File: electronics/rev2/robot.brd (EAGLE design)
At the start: 170.3 x 155.9 mm, 93 parts, among them J1 USB-B, J3 B6B-ZR, J4 B6B-ZR, J5 B6B-ZR, J6 KICKER, Q1 IRLMS2002TRPBF, Q2 IRLMS2002TRPBF, Q3 NPN_BC817,215, Q4 SUD50N04-8M8P-4GE3, Q5 NPN_BC817,215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

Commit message: Re-camming, minor renamings
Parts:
- renumbered U$1 to SW1, U$12 to U11, U$13 to U12, U$25 to U8, U$7 to U10
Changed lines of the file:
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@@
 <attribute name="VALUE" value="0.3" x="-10.16" y="-65.5574" size="1.778" layer="27" display="off"/>
 </element>
-<element name="U$25" library="rhoban" package="SOT223" value="TS2940CW-3.3RP" x="7.4676" y="7.7724" rot="R90">
+<element name="U8" library="rhoban" package="SOT223" value="TS2940CW-3.3RP" x="7.4676" y="7.7724" rot="R90">
 <attribute name="FARNELL" value="7261403" x="-3.0734" y="0.5588" size="1.778" layer="27" rot="R90" display="off"/>
 </element>
@@
 <attribute name="VALUE" value="0.33µF" x="26.3144" y="14.7066" size="1.778" layer="27" rot="R180" display="off"/>
 </element>
-<element name="U$1" library="rhoban" package="L102011ML04Q" value="L102011ML04Q" x="39.1409125" y="18.7719375" rot="R210">
+<element name="SW1" library="rhoban" package="L102011ML04Q" value="L102011ML04Q" x="39.1409125" y="18.7719375" rot="R210">
 <attribute name="FARNELL" value="2931770" x="39.1409125" y="18.7719375" size="1.778" layer="27" rot="R210" display="off"/>
 </element>
-<element name="U$7" library="rhoban" package="HSOP8" value="TB67H450FNG" x="4.159615625" y="-10.26823125"/>
+<element name="U10" library="rhoban" package="HSOP8" value="TB67H450FNG" x="4.159615625" y="-10.26823125"/>
 <element name="R19" library="rcl" package="R1206" value="0.33" x="6.593578125" y="-3.92773125"/>
-<element name="U$12" library="rhoban" package="HSOP8" value="TB67H450FNG" x="-7.65661875" y="0.71041875"/>
+<element name="U11" library="rhoban" package="HSOP8" value="TB67H450FNG" x="-7.65661875" y="0.71041875"/>
 <element name="R20" library="rcl" package="R1206" value="0.33" x="-6.08386875" y="7.10789375"/>
-<element name="U$13" library="rhoban" package="HSOP8" value="TB67H450FNG" x="-39.524309375" y="7.266759375" rot="R210"/>
+<element name="U12" library="rhoban" package="HSOP8" value="TB67H450FNG" x="-39.524309375" y="7.266759375" rot="R210"/>
 <element name="R21" library="rcl" package="R1206" value="0.33" x="-37.80135625" y="1.564721875" rot="R210"/>
 <element name="C18" library="SparkFun-Capacitors" package="0805" value="1µF" x="7.802584375" y="-8.766778125" rot="R270">
@@
 <contactref element="C9" pad="2"/>
 <contactref element="C12" pad="2"/>
-<contactref element="U$25" pad="2"/>
-<contactref element="U$25" pad="2"/>
+<contactref element="U8" pad="2"/>
+<contactref element="U8" pad="2"/>
 <contactref element="C13" pad="2"/>
 <contactref element="C14" pad="2"/>
 <contactref element="U1" pad="26"/>
-<contactref element="U$7" pad="1"/>
+<contactref element="U10" pad="1"/>
 <contactref element="R19" pad="2"/>
-<contactref element="U$12" pad="1"/>
+<contactref element="U11" pad="1"/>
 <contactref element="R20" pad="2"/>
-<contactref element="U$13" pad="1"/>
+<contactref element="U12" pad="1"/>
 <contactref element="R21" pad="2"/>
 <contactref element="C18" pad="2"/>
@@
 <contactref element="C3" pad="1"/>
 <contactref element="C17" pad="1"/>
-<contactref element="U$1" pad="P$1"/>
-<contactref element="U$7" pad="5"/>
-<contactref element="U$12" pad="5"/>
-<contactref element="U$13" pad="5"/>
+<contactref element="SW1" pad="P$1"/>
+<contactref element="U10" pad="5"/>
+<contactref element="U11" pad="5"/>
+<contactref element="U12" pad="5"/>
 <contactref element="C18" pad="1"/>
 <contactref element="C21" pad="1"/>
@@
 <signal name="M1A">
 <contactref element="U2" pad="16"/>
-<contactref element="U$7" pad="3"/>
+<contactref element="U10" pad="3"/>
 <wire x1="4.2926" y1="-22.7004" x2="4.2926" y2="-16.93053125" width="0.4064" layer="1"/>
 <wire x1="4.2926" y1="-16.93053125" x2="4.572" y2="-16.256" width="0.4064" layer="1" curve="-45"/>
@@
 <signal name="M1B">
 <contactref element="U2" pad="13"/>
-<contactref element="U$7" pad="2"/>
+<contactref element="U10" pad="2"/>
 <wire x1="3.524615625" y1="-12.86823125" x2="3.556" y2="-12.944" width="0.4064" layer="1" curve="-45"/>
 <wire x1="3.556" y1="-12.944" x2="3.556" y2="-14.986" width="0.4064" layer="1"/>
@@
 <signal name="M2P2" class="1">
 <contactref element="J4" pad="1"/>
-<contactref element="U$12" pad="8"/>
+<contactref element="U11" pad="8"/>
 <wire x1="-9.56161875" y1="3.31041875" x2="-9.525" y2="4.064" width="0.4064" layer="1"/>
 <wire x1="-9.525" y1="4.064" x2="-9.652" y2="6.096" width="0.4064" layer="1" curve="12.716635"/>
@@
 <signal name="M2A">
 <contactref element="U2" pad="28"/>
-<contactref element="U$12" pad="3"/>
+<contactref element="U11" pad="3"/>
 <wire x1="-7.02161875" y1="-1.88958125" x2="-7.02161875" y2="-3.64638125" width="0.4064" layer="1"/>
 <wire x1="-7.02161875" y1="-3.64638125" x2="-6.985" y2="-3.556" width="0.4064" layer="1"/>
@@
 <signal name="M2B">
 <contactref element="U2" pad="30"/>
-<contactref element="U$12" pad="2"/>
+<contactref element="U11" pad="2"/>
 <wire x1="-8.29161875" y1="-1.88958125" x2="-8.29161875" y2="-3.59261875" width="0.4064" layer="1"/>
 <wire x1="-8.29161875" y1="-3.59261875" x2="-8.382" y2="-3.556" width="0.4064" layer="1"/>
@@
 <signal name="M3A">
 <contactref element="U2" pad="36"/>
-<contactref element="U$13" pad="3"/>
+<contactref element="U12" pad="3"/>
 <wire x1="-41.374234375" y1="9.200925" x2="-42.037" y2="10.414" width="0.4064" layer="1"/>
 <via x="-42.037" y="10.414" extent="1-16" drill="0.3" diameter="0.7" shape="octagon"/>
@@
 <signal name="M3B">
 <contactref element="U2" pad="37"/>
-<contactref element="U$13" pad="2"/>
+<contactref element="U12" pad="2"/>
 <via x="-40.894" y="11.049" extent="1-16" drill="0.3" diameter="0.7" shape="octagon"/>
 <wire x1="-40.894" y1="11.176" x2="-40.5351375" y2="10.273815625" width="0.4064" layer="16"/>
@@
 <contactref element="C5" pad="1"/>
 <contactref element="C6" pad="1"/>
-<contactref element="U$25" pad="1"/>
+<contactref element="U8" pad="1"/>
 <contactref element="D3" pad="1"/>
 <wire x1="-1.662" y1="70.993" x2="-5.08" y2="70.993" width="0.4064" layer="1"/>
@@
 <signal name="M1P1" class="1">
 <contactref element="J3" pad="6"/>
-<contactref element="U$7" pad="6"/>
+<contactref element="U10" pad="6"/>
 <wire x1="4.794615625" y1="-7.66823125" x2="4.794615625" y2="-6.762384375" width="0.4064" layer="1"/>
 <wire x1="4.794615625" y1="-6.762384375" x2="5.969" y2="-5.588" width="0.4064" layer="1" curve="-90"/>
@@
 <signal name="M1P2" class="1">
 <contactref element="J3" pad="1"/>
-<contactref element="U$7" pad="8"/>
+<contactref element="U10" pad="8"/>
 <wire x1="2.254615625" y1="-7.66823125" x2="2.254615625" y2="-5.111384375" width="0.4064" layer="1"/>
 <wire x1="2.254615625" y1="-5.111384375" x2="5.969" y2="-1.524" width="0.4064" layer="1" curve="-90"/>
@@
 <signal name="M2P1" class="1">
 <contactref element="J4" pad="6"/>
-<contactref element="U$12" pad="6"/>
+<contactref element="U11" pad="6"/>
 <wire x1="-7.02161875" y1="3.31041875" x2="-6.985" y2="4.445" width="0.4064" layer="1"/>
 <wire x1="-6.985" y1="4.445" x2="-6.223" y2="5.08" width="0.4064" layer="1" curve="-96.691545"/>
@@
 <signal name="M3P2" class="1">
 <contactref element="J5" pad="1"/>
-<contactref element="U$13" pad="8"/>
+<contactref element="U12" pad="8"/>
 <wire x1="-36.574528125" y1="5.967590625" x2="-33.37213125" y2="0.420871875" width="0.4064" layer="1"/>
 <wire x1="-33.37213125" y1="0.420871875" x2="-33.386109375" y2="0.368690625" width="0.4064" layer="1"/>
@@
 <signal name="M3P1" class="1">
 <contactref element="J5" pad="6"/>
-<contactref element="U$13" pad="6"/>
+<contactref element="U12" pad="6"/>
 <wire x1="-38.774234375" y1="4.697590625" x2="-38.227" y2="3.81" width="0.4064" layer="1"/>
 <wire x1="-38.227" y1="3.81" x2="-38.481" y2="3.048" width="0.4064" layer="1" curve="-100.18061"/>
@@
 <contactref element="C14" pad="1"/>
 <contactref element="C13" pad="1"/>
-<contactref element="U$25" pad="3"/>
+<contactref element="U8" pad="3"/>
 <contactref element="B1" pad="P$2"/>
 <contactref element="J3" pad="2"/>
 <contactref element="J4" pad="2"/>
 <contactref element="J5" pad="2"/>
-<contactref element="U$7" pad="4"/>
-<contactref element="U$12" pad="4"/>
-<contactref element="U$13" pad="4"/>
+<contactref element="U10" pad="4"/>
+<contactref element="U11" pad="4"/>
+<contactref element="U12" pad="4"/>
 <wire x1="10.5664" y1="10.0838" x2="12.875346875" y2="10.0838" width="0.6096" layer="1"/>
 <wire x1="12.875346875" y1="10.0838" x2="13.462" y2="9.8408" width="0.6096" layer="1" curve="-45"/>
@@
 <signal name="N$7" class="1">
 <contactref element="J2" pad="2"/>
-<contactref element="U$1" pad="P$2"/>
+<contactref element="SW1" pad="P$2"/>
 <wire x1="17.9947625" y1="18.074834375" x2="19.608809375" y2="16.4607875" width="1.016" layer="16"/>
 <wire x1="19.608809375" y1="16.4607875" x2="21.023025" y2="15.875" width="1.016" layer="16" curve="45.00009"/>
@@
 </signal>
 <signal name="N$18" class="1">
-<contactref element="U$7" pad="7"/>
+<contactref element="U10" pad="7"/>
 <contactref element="R19" pad="1"/>
 <wire x1="3.524615625" y1="-7.66823125" x2="3.524615625" y2="-7.6457625" width="0.4064" layer="1"/>
@@
 </signal>
 <signal name="N$20" class="1">
-<contactref element="U$12" pad="7"/>
+<contactref element="U11" pad="7"/>
 <contactref element="R20" pad="1"/>
 <wire x1="-8.29161875" y1="3.31041875" x2="-8.255" y2="4.318" width="0.4064" layer="1"/>
@@
 </signal>
 <signal name="N$21" class="1">
-<contactref element="U$13" pad="7"/>
+<contactref element="U12" pad="7"/>
 <contactref element="R21" pad="1"/>
 <wire x1="-37.67438125" y1="5.332590625" x2="-36.83" y2="3.81" width="0.4064" layer="1"/>

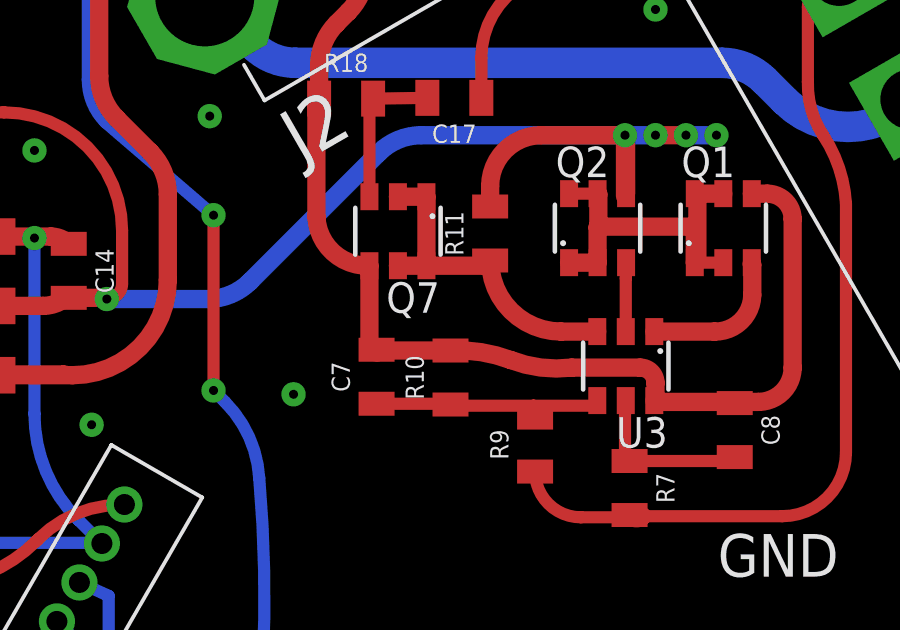
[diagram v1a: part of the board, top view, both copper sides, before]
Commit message: Adding D2 diode
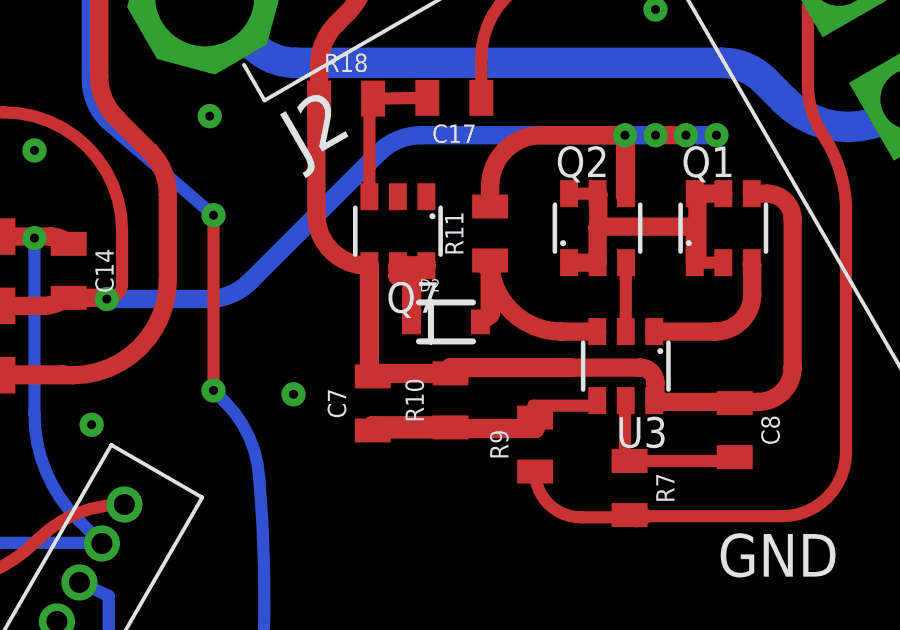
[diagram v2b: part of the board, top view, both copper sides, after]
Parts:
- added D2: (no value), SparkFun-DiscreteSemi:SOD-323
- moved C7 0.90 mm to (23.6, 4.52)
- moved R10 0.76 mm to (26.2, 4.62)
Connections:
- new net N$22: D2.1, Q7.1, Q7.2, Q7.5, Q7.6
- net N$13: now also D2.2; no longer Q7.1, Q7.2, Q7.5, Q7.6
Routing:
- net N$13: track 10.9 -> 7.00 mm
- net N$22: track 0.00 -> 3.28 mm
- net GND_RAW: track 38.8 -> 39.7 mm
- net N$9: track 7.94 -> 8.65 mm
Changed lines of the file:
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@@
 <attribute name="FARNELL" value="2074334RL" x="29.0068" y="3.1496" size="1.778" layer="27" rot="R90" display="off"/>
 </element>
-<element name="R10" library="SparkFun-Resistors" package="0805" value="470" x="26.1874" y="5.3848" rot="R90">
-<attribute name="PROD_ID" value="RES-11622" x="26.1874" y="5.3848" size="1.778" layer="27" rot="R90" display="off"/>
-<attribute name="VALUE" value="0.3" x="26.1874" y="5.3848" size="1.778" layer="27" rot="R90" display="off"/>
-<attribute name="FARNELL" value="2074334RL" x="26.1874" y="5.3848" size="1.778" layer="27" rot="R90" display="off"/>
+<element name="R10" library="SparkFun-Resistors" package="0805" value="470" x="26.1874" y="4.6228" rot="R90">
+<attribute name="PROD_ID" value="RES-11622" x="26.1874" y="4.6228" size="1.778" layer="27" rot="R90" display="off"/>
+<attribute name="VALUE" value="0.3" x="26.1874" y="4.6228" size="1.778" layer="27" rot="R90" display="off"/>
+<attribute name="FARNELL" value="2074334RL" x="26.1874" y="4.6228" size="1.778" layer="27" rot="R90" display="off"/>
 </element>
 <element name="R11" library="SparkFun-Resistors" package="0805" value="2K" x="27.5082" y="10.1854" rot="R90">
@@
 <attribute name="FARNELL" value="2688486RL" x="-0.762" y="70.993" size="1.778" layer="27" display="off"/>
 </element>
-<element name="C7" library="SparkFun-Capacitors" package="0805" value="0.1µF" x="23.7236" y="5.4102" rot="R90">
-<attribute name="PROD_ID" value="CAP-08469" x="23.7236" y="5.7912" size="1.778" layer="27" rot="R90" display="off"/>
-<attribute name="VALUE" value="0.33µF" x="23.7236" y="5.7912" size="1.778" layer="27" rot="R90" display="off"/>
-<attribute name="FARNELL" value="2688486RL" x="23.7236" y="5.4102" size="1.778" layer="27" rot="R90" display="off"/>
+<element name="C7" library="SparkFun-Capacitors" package="0805" value="0.1µF" x="23.5966" y="4.5212" rot="R90">
+<attribute name="PROD_ID" value="CAP-08469" x="23.5966" y="4.9022" size="1.778" layer="27" rot="R90" display="off"/>
+<attribute name="VALUE" value="0.33µF" x="23.5966" y="4.9022" size="1.778" layer="27" rot="R90" display="off"/>
+<attribute name="FARNELL" value="2688486RL" x="23.5966" y="4.5212" size="1.778" layer="27" rot="R90" display="off"/>
 </element>
 <element name="C8" library="SparkFun-Capacitors" package="0805" value="0.1µF" x="35.6616" y="3.6322" rot="R270">
@@
 <attribute name="PROD_ID" value="RES-11622" x="3.175" y="-17.018" size="1.778" layer="27" rot="R180" display="off"/>
 <attribute name="VALUE" value="0.3" x="3.175" y="-17.018" size="1.778" layer="27" rot="R180" display="off"/>
+</element>
+<element name="D2" library="SparkFun-DiscreteSemi" package="SOD-323" value="" x="26.035" y="7.239">
+<attribute name="FARNELL" value="8737843RL" x="22.86" y="10.795" size="1.778" layer="27" display="off"/>
 </element>
 </elements>
@@
 <wire x1="21.717" y1="14.466321875" x2="21.717" y2="10.7524" width="0.6096" layer="1"/>
 <wire x1="21.717" y1="10.7524" x2="23.4848" y2="9.1116" width="0.6096" layer="1" curve="90"/>
-<wire x1="23.4848" y1="9.1116" x2="23.4848" y2="6.4872" width="0.6096" layer="1"/>
-<wire x1="23.4848" y1="6.4872" x2="23.749" y2="6.223" width="0.6096" layer="1" curve="90"/>
-<wire x1="23.749" y1="6.223" x2="23.876" y2="6.35" width="0.6096" layer="1" curve="-90"/>
-<wire x1="23.7634" y1="6.35" x2="23.749" y2="6.35" width="0.6096" layer="1"/>
-<wire x1="23.7236" y1="6.3102" x2="23.7634" y2="6.35" width="0.6096" layer="1" curve="-90"/>
-<wire x1="23.7634" y1="6.35" x2="23.876" y2="6.35" width="0.6096" layer="1"/>
-<wire x1="23.876" y1="6.35" x2="23.9412" y2="6.2848" width="0.6096" layer="1" curve="90"/>
-<wire x1="23.9412" y1="6.2848" x2="26.1874" y2="6.2848" width="0.6096" layer="1"/>
-<wire x1="26.1874" y1="6.2848" x2="28.194" y2="5.969" width="0.6096" layer="1" curve="-23.449055"/>
-<wire x1="28.194" y1="5.969" x2="30.226" y2="5.715" width="0.6096" layer="1" curve="27.973536"/>
 <wire x1="30.226" y1="5.715" x2="32.512" y2="5.715" width="0.6096" layer="1"/>
 <wire x1="32.512" y1="5.715" x2="33.02" y2="5.207" width="0.6096" layer="1" curve="-90"/>
@@
 <wire x1="36.449" y1="4.572" x2="35.7014" y2="4.572" width="0.6096" layer="1"/>
 <wire x1="35.7014" y1="4.572" x2="35.6616" y2="4.5322" width="0.6096" layer="1" curve="90"/>
+<wire x1="26.1874" y1="5.5228" x2="23.5966" y2="5.5228" width="0.64" layer="1"/>
+<wire x1="23.5966" y1="5.5228" x2="23.5966" y2="5.4212" width="0.64" layer="1"/>
+<wire x1="23.5966" y1="5.4212" x2="23.4848" y2="5.4212" width="0.64" layer="1"/>
+<wire x1="23.4848" y1="5.4212" x2="23.4848" y2="9.1116" width="0.64" layer="1"/>
+<wire x1="30.226" y1="5.715" x2="26.1874" y2="5.715" width="0.64" layer="1"/>
+<wire x1="26.1874" y1="5.715" x2="26.1874" y2="5.5228" width="0.64" layer="1"/>
 </signal>
 <signal name="N$7" class="1">
@@
 <contactref element="R10" pad="1"/>
 <contactref element="C7" pad="1"/>
-<wire x1="26.2272" y1="4.445" x2="28.956" y2="4.445" width="0.4064" layer="1"/>
 <wire x1="28.956" y1="4.445" x2="30.9086" y2="4.445" width="0.4064" layer="1"/>
 <wire x1="30.9086" y1="4.445" x2="31.0794" y2="4.6158" width="0.4064" layer="1" curve="90"/>
-<wire x1="23.7236" y1="4.5102" x2="26.1002" y2="4.5102" width="0.4064" layer="1"/>
-<wire x1="26.1002" y1="4.5102" x2="26.162" y2="4.572" width="0.4064" layer="1" curve="90"/>
-<wire x1="26.1874" y1="4.4848" x2="26.1256" y2="4.4848" width="0.4064" layer="1"/>
-<wire x1="26.1256" y1="4.4848" x2="26.1002" y2="4.5102" width="0.4064" layer="1" curve="-90"/>
-<wire x1="26.2272" y1="4.445" x2="26.1874" y2="4.4848" width="0.4064" layer="1" curve="-90"/>
+<wire x1="26.1002" y1="3.683" x2="26.1874" y2="3.7228" width="0.4064" layer="1" curve="-90"/>
 <wire x1="29.0068" y1="4.0496" x2="28.956" y2="4.445" width="0.4064" layer="1"/>
+<wire x1="26.1874" y1="3.7228" x2="23.5966" y2="3.7228" width="0.75" layer="1"/>
+<wire x1="23.5966" y1="3.7228" x2="23.5966" y2="3.6212" width="0.75" layer="1"/>
+<wire x1="26.1002" y1="3.683" x2="29.0068" y2="3.683" width="0.64" layer="1"/>
+<wire x1="29.0068" y1="3.683" x2="29.0068" y2="4.0496" width="0.64" layer="1"/>
 </signal>
 <signal name="N$10">
@@
 <contactref element="R11" pad="1"/>
 <contactref element="U3" pad="3"/>
-<contactref element="Q7" pad="2"/>
-<contactref element="Q7" pad="6"/>
-<contactref element="Q7" pad="1"/>
-<contactref element="Q7" pad="5"/>
-<wire x1="24.4348" y1="9.1116" x2="25.3848" y2="9.1116" width="0.6096" layer="1"/>
-<wire x1="24.4348" y1="11.4116" x2="25.3848" y2="11.4116" width="0.6096" layer="1"/>
-<wire x1="25.3848" y1="11.4116" x2="25.3848" y2="9.1116" width="0.6096" layer="1"/>
 <wire x1="31.0794" y1="6.9158" x2="29.8778" y2="6.9158" width="0.6096" layer="1"/>
 <wire x1="29.8778" y1="6.9158" x2="27.5082" y2="9.2854" width="0.6096" layer="1" curve="-90"/>
-<wire x1="25.3848" y1="9.1116" x2="27.3344" y2="9.1116" width="0.6096" layer="1"/>
 <wire x1="27.3344" y1="9.1116" x2="27.5082" y2="9.2854" width="0.6096" layer="1" curve="90"/>
+<contactref element="D2" pad="2"/>
+<wire x1="27.185" y1="7.239" x2="27.5082" y2="7.493" width="0.64" layer="1"/>
+<wire x1="27.5082" y1="7.493" x2="27.5082" y2="9.2854" width="0.64" layer="1"/>
 </signal>
 <signal name="N$6">
@@
 <wire x1="-36.83" y1="3.81" x2="-36.569865625" y2="2.275721875" width="0.4064" layer="1" curve="-38.776909"/>
 </signal>
+<signal name="N$22">
+<contactref element="D2" pad="1"/>
+<contactref element="Q7" pad="1"/>
+<contactref element="Q7" pad="5"/>
+<contactref element="Q7" pad="2"/>
+<contactref element="Q7" pad="6"/>
+<wire x1="24.4348" y1="9.1116" x2="25.3848" y2="9.1116" width="0.64" layer="1"/>
+<wire x1="24.4348" y1="11.4116" x2="25.3848" y2="11.4116" width="0" layer="19" extent="1-1"/>
+<wire x1="25.3848" y1="9.1116" x2="25.3848" y2="11.4116" width="0" layer="19" extent="1-1"/>
+<wire x1="24.885" y1="7.239" x2="24.892" y2="7.493" width="0.64" layer="1"/>
+<wire x1="24.892" y1="7.493" x2="24.892" y2="8.763" width="0.64" layer="1"/>
+<wire x1="24.892" y1="8.763" x2="24.4348" y2="8.763" width="0.64" layer="1"/>
+<wire x1="24.4348" y1="8.763" x2="24.4348" y2="9.1116" width="0.64" layer="1"/>
+</signal>
 </signals>
